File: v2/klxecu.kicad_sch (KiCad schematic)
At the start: 15 parts, among them J1 CAM_SENSOR_IN, J4 Conn_01x06, U1 S36B-WPZK-A, U2 LM2940S-5.0/NOPB, U3 Arduino Mega 2560 Pro, U4 ATtiny84-20P

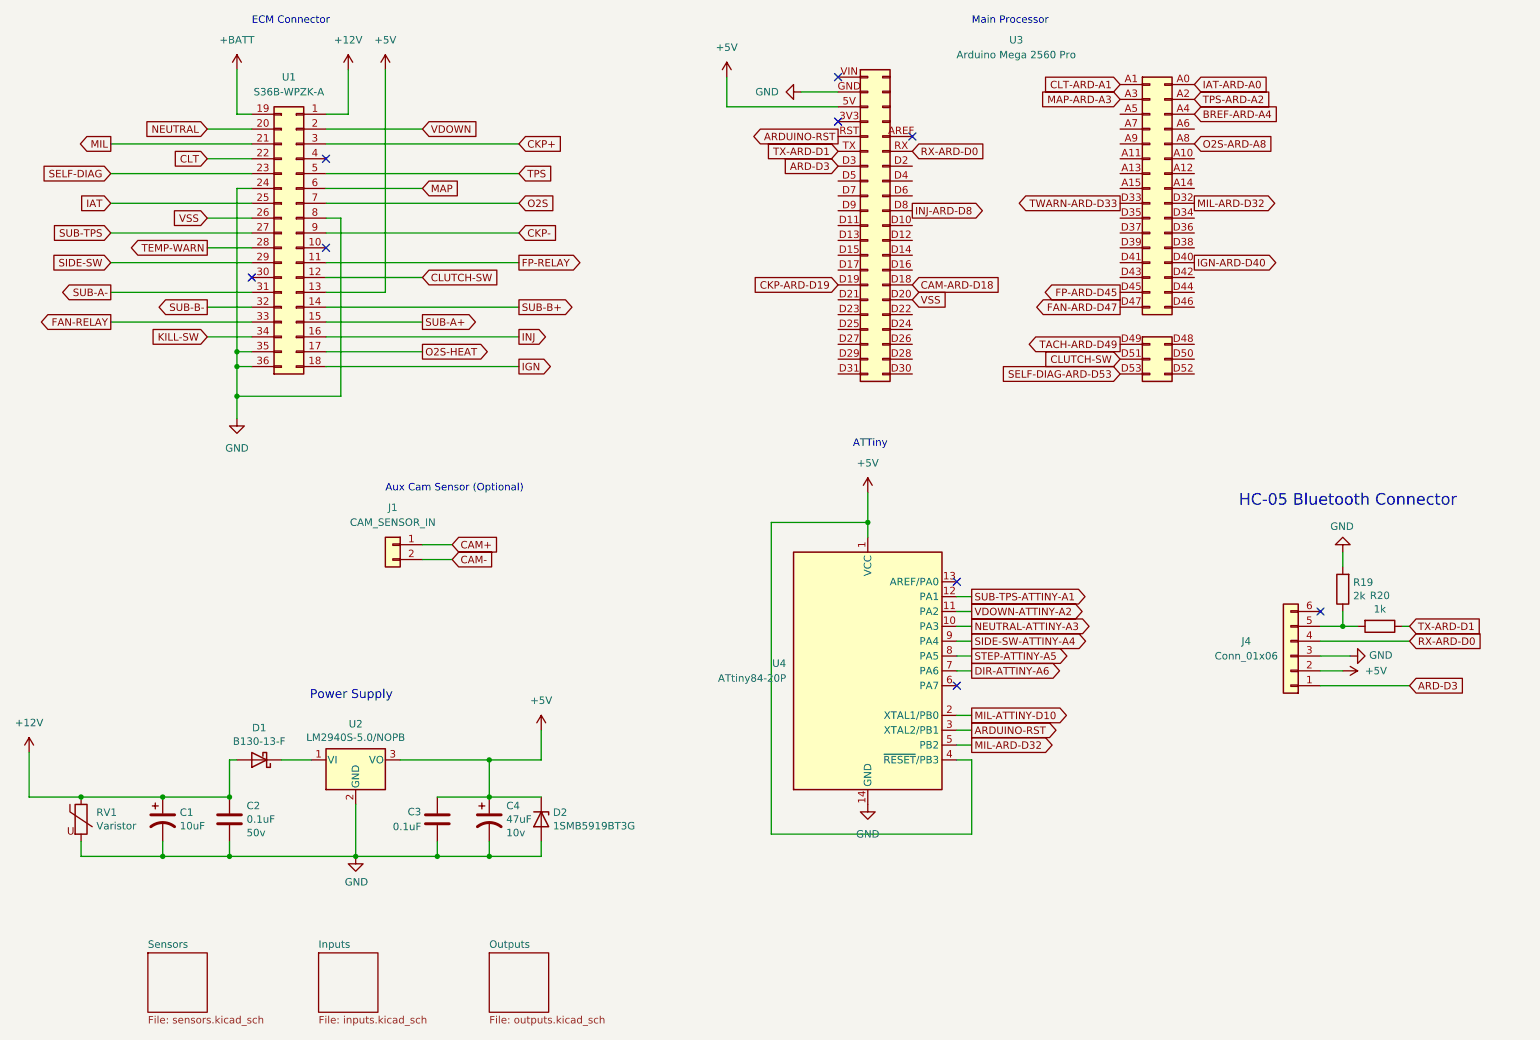
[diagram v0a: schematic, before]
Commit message: Delete ATTiny and associated circuitry
Control the secondary throttle w/ open loop stepper idle control in the speeduino firmware
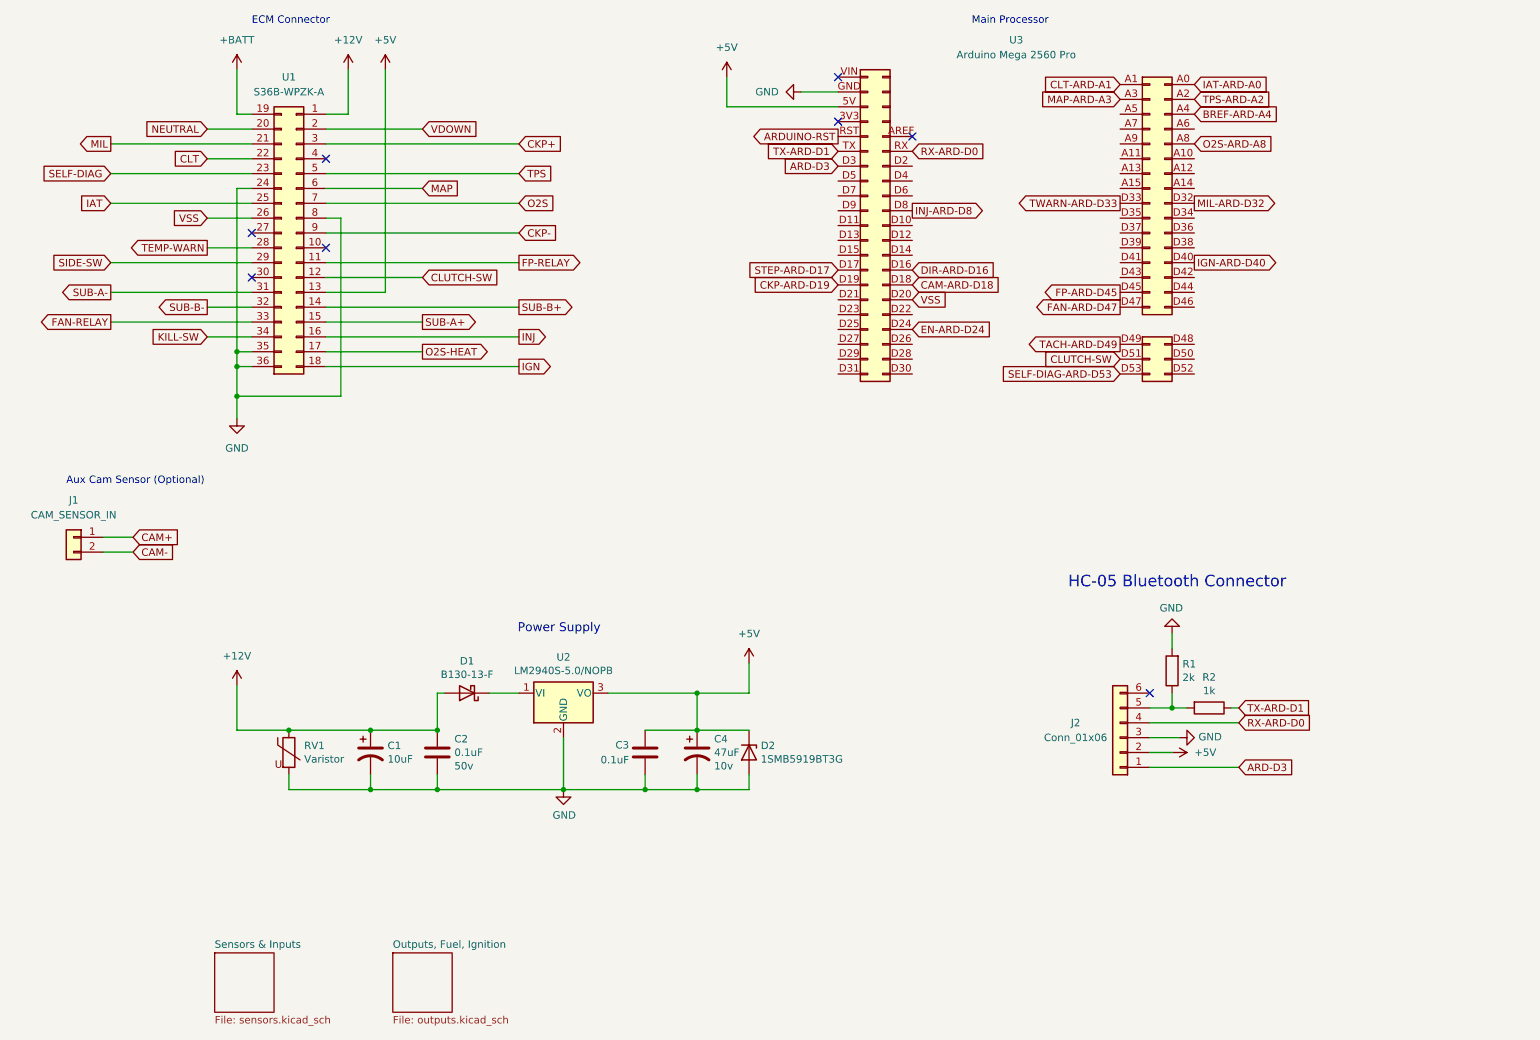
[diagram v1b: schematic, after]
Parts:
- removed U4: ATtiny84-20P, Package_DIP:DIP-14_W7.62mm, symbol MCU_Microchip_ATtiny:ATtiny84-20P
- renumbered J4 to J2, R19 to R1, R20 to R2
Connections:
- net DIR-ARD-D16: now reaches U3.D16
- net STEP-ARD-D17: now reaches U3.D17
- net EN-ARD-D24: now reaches U3.D24
- net SUB-TPS: no longer names the net of U1.27
- no-connect marks 9 -> 8
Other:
- sheet Outputs renamed Outputs, Fuel, Ignition
- sheet Sensors renamed Sensors & Inputs
- removed sheet Inputs
- note removed: "ATTiny"
- moved on the sheet: C1, C2, C3, C4, D1, D2, J1, J2, R1, R2, RV1, U2

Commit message: V2.1 is done?
Uses the JST WPZ connector footprint instead of standard
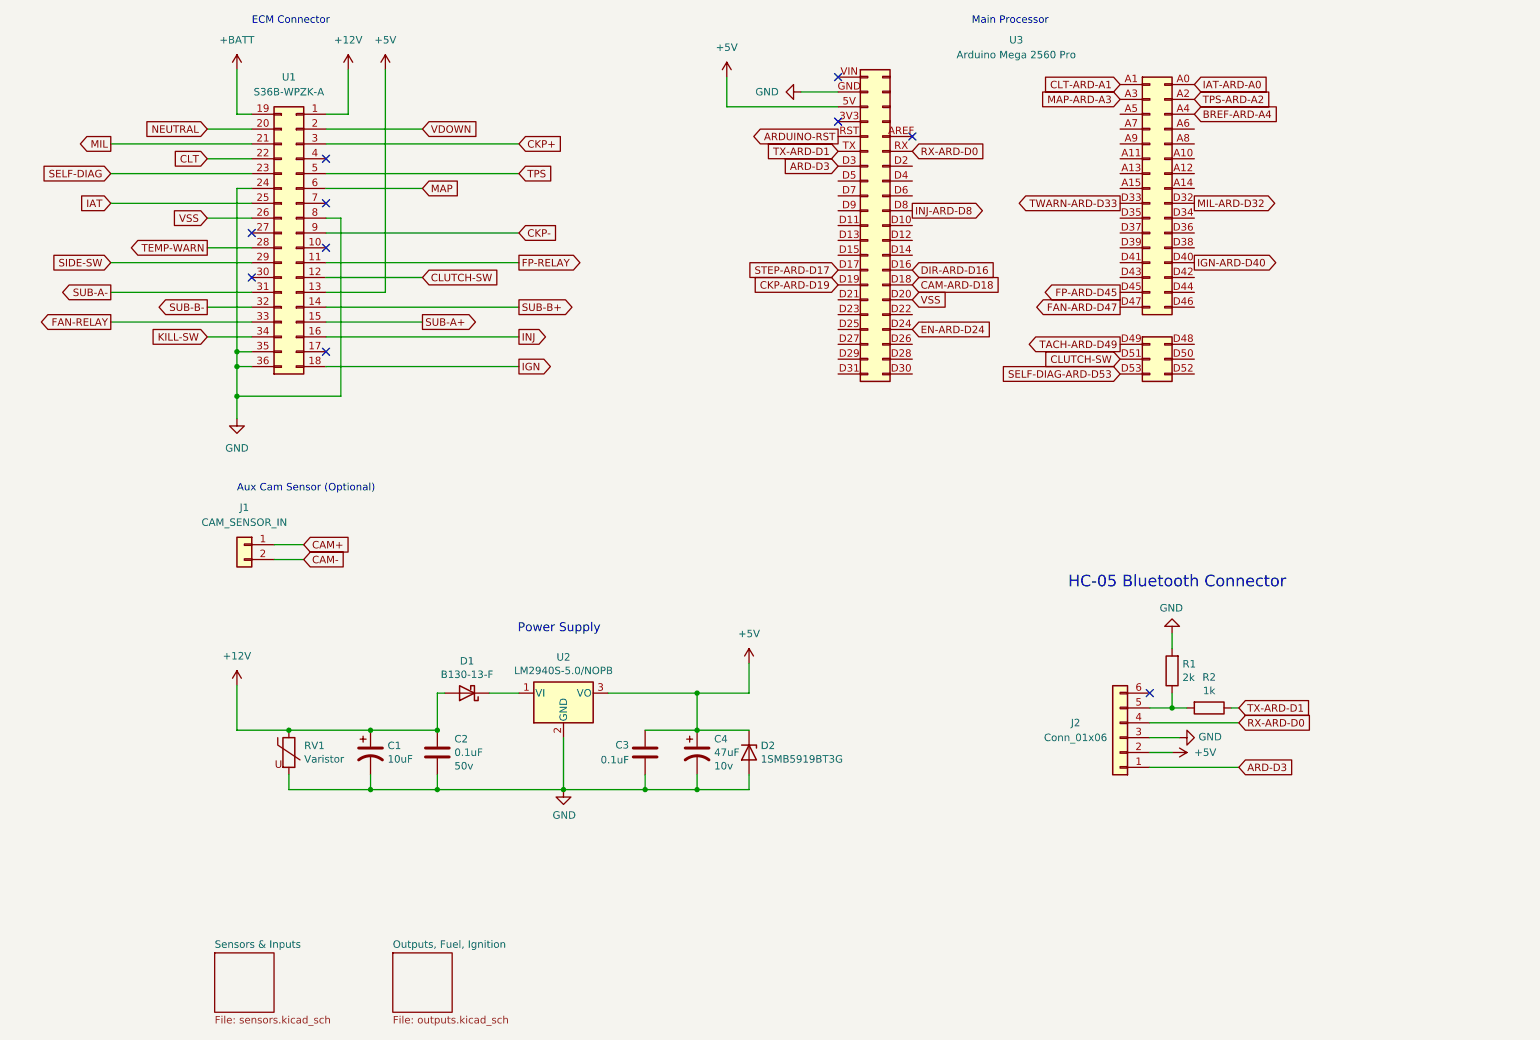
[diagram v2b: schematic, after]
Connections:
- net O2S: no longer names the net of U1.7
- net O2S-ARD-A8: no longer names the net of U3.A8
- net O2S-HEAT: no longer names the net of U1.17
- no-connect marks 8 -> 10
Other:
- moved on the sheet: J1

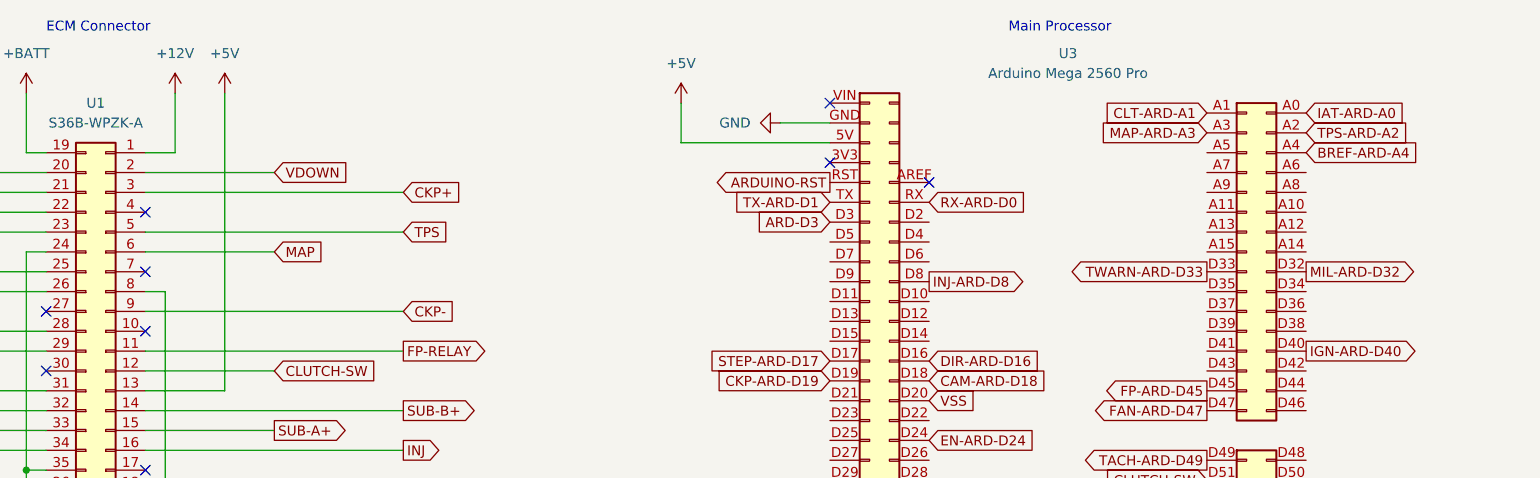
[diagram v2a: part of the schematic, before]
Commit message: Re-add traces for oxygen sensor
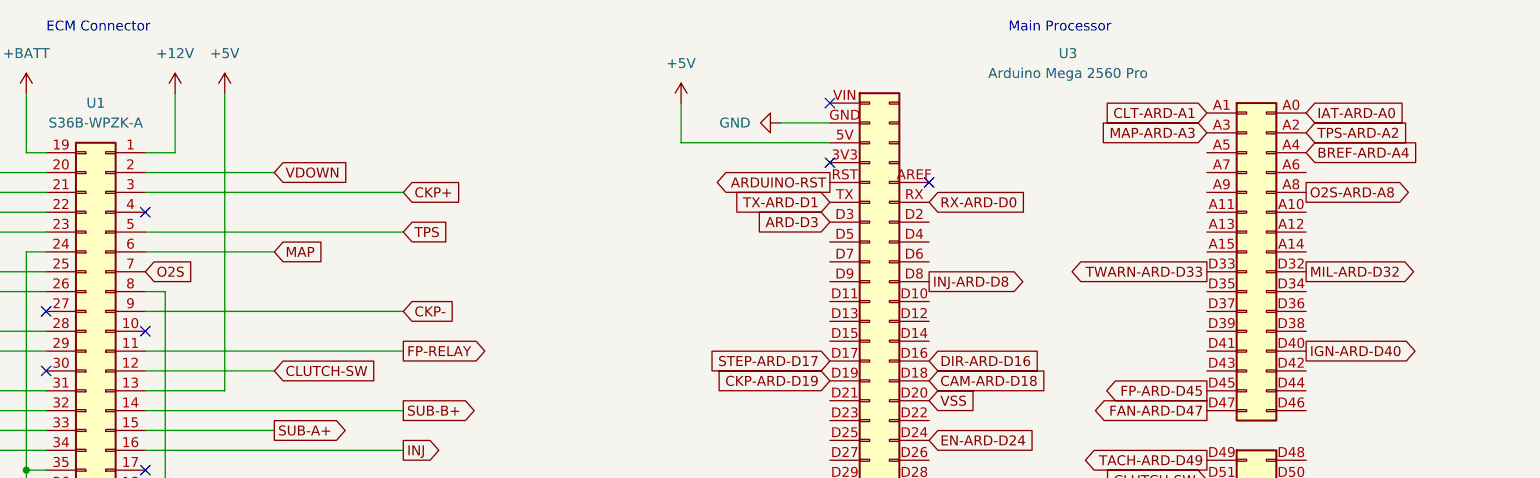
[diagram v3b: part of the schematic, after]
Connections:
- net O2S: now reaches U1.7
- net O2S-ARD-A8: now reaches U3.A8
- no-connect marks 10 -> 9
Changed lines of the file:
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@@
   (no_connect (at 171.45 36.83))
   (no_connect (at 158.75 26.67))
-  (no_connect (at 71.12 48.26))
   (no_connect (at 158.75 34.29))
   (no_connect (at 58.42 53.34))
@@
     )
   )
+  (global_label "O2S" (shape input) (at 71.12 48.26 0) (fields_autoplaced)
+    (effects (font (size 1.27 1.27)) (justify left))
+    (property "Intersheet References" "${INTERSHEET_REFS}" (id 0) (at 77.2826 48.3394 0)
+      (effects (font (size 1.27 1.27)) (justify left) hide)
+    )
+  )
   (global_label "CKP-" (shape input) (at 104.14 53.34 0) (fields_autoplaced)
     (effects (font (size 1.27 1.27)) (justify left))
@@
     (effects (font (size 1.27 1.27)) (justify left))
     (property "Intersheet References" "${INTERSHEET_REFS}" (id 0) (at 186.805 69.7706 0)
+      (effects (font (size 1.27 1.27)) (justify left) hide)
+    )
+  )
+  (global_label "O2S-ARD-A8" (shape output) (at 219.71 38.1 0) (fields_autoplaced)
+    (effects (font (size 1.27 1.27)) (justify left))
+    (property "Intersheet References" "${INTERSHEET_REFS}" (id 0) (at 234.9441 38.0206 0)
       (effects (font (size 1.27 1.27)) (justify left) hide)
     )
@@
       (reference "#PWR047") (unit 1) (value "GND") (footprint "")
     )
+    (path "/98f72596-e058-4dba-8464-025a303cdc65/ba3a3e4f-d4a5-47f8-af26-edcfc7202ede"
+      (reference "#PWR?") (unit 1) (value "GND") (footprint "")
+    )
     (path "/a01c941e-2669-451e-92d9-4d3556674fec/75126fec-323d-4a00-8d28-b0141aa312d7"
       (reference "A1") (unit 1) (value "Pololu_Breakout_A4988") (footprint "Module:Pololu_Breakout-16_15.2x20.3mm")
@@
       (reference "C21") (unit 1) (value "100uF") (footprint "Capacitor_THT:CP_Radial_D5.0mm_P2.50mm")
     )
+    (path "/98f72596-e058-4dba-8464-025a303cdc65/836826c5-a09c-468c-b76a-db846e15572a"
+      (reference "C?") (unit 1) (value "0.33uF") (footprint "Capacitor_SMD:C_0805_2012Metric_Pad1.18x1.45mm_HandSolder")
+    )
+    (path "/98f72596-e058-4dba-8464-025a303cdc65/db86639b-6847-44b0-bd56-1d0ca68cc2d0"
+      (reference "C?") (unit 1) (value "100nF") (footprint "Capacitor_SMD:C_0805_2012Metric_Pad1.18x1.45mm_HandSolder")
+    )
     (path "/f8dcc113-360c-4a3f-b3ce-db2657bf4383"
       (reference "D1") (unit 1) (value "B130-13-F") (footprint "Diode_SMD:D_SMA")
@@
       (reference "R21") (unit 1) (value "10K") (footprint "Resistor_SMD:R_0805_2012Metric")
     )
+    (path "/98f72596-e058-4dba-8464-025a303cdc65/1b734947-4591-44d6-ba02-cd89adc71133"
+      (reference "R?") (unit 1) (value "470") (footprint "Resistor_SMD:R_0805_2012Metric_Pad1.20x1.40mm_HandSolder")
+    )
     (path "/e7efca28-0eae-4ec9-be91-e1da3a3f1517"
